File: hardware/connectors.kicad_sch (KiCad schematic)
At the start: 0 parts

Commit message: connectors - added, buses - todo
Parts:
- added J3: PWM1, symbol Connector_Generic:Conn_01x03
- added J5: PWM2, symbol Connector_Generic:Conn_01x03
- added J6: POWER & CAN & SPI2, symbol Connector_Generic:Conn_02x10_Top_Bottom
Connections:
- new net +5V: J3.3 (Pin_3), J5.3 (Pin_3)
- new net +6V6S1: J6.6 (Pin_6)
- new net +6V6S2: J6.7 (Pin_7)
- new net CAN_H: J6.14 (Pin_14)
- new net CAN_L: J6.4 (Pin_4)
- new net GND: J3.1 (Pin_1), J5.1 (Pin_1), J6.10 (Pin_10), J6.18 (Pin_18), J6.19 (Pin_19), J6.20 (Pin_20)
- new net PWM1: J3.2 (Pin_2)
- new net SPI2_MISO: J6.9 (Pin_9)
- new net SPI2_MOSI: J6.8 (Pin_8)
- new net SPI2_SCK: J6.16 (Pin_16)
- new net VCC: J6.1 (Pin_1), J6.11 (Pin_11), J6.12 (Pin_12), J6.13 (Pin_13), J6.2 (Pin_2), J6.3 (Pin_3)
- no-connect marks 0 -> 3
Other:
- note added: "POWER & CAN & SPI2"
- note added: "PWM"

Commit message: Poprawione busy, brak errorow
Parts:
- removed J6: POWER & CAN & SPI2, symbol Connector_Generic:Conn_02x10_Top_Bottom
- added C18: 10n, Capacitor_SMD:C_0603_1608Metric_Pad1.08x0.95mm_HandSolder, symbol Device:C_Small
- added J1: USB_C_Receptacle_USB2.0_14P, symbol Connector:USB_C_Receptacle_USB2.0_14P
- added J2: FTSH-107-01-L-DV-K-A, FTSH-107-XX-YYY-DV-K-A, symbol FTSH-107-01-L-DV-K-A:FTSH-107-01-L-DV-K-A
- added J7: POWER & CAN & SPI2, symbol Connector_Generic:Conn_02x06_Odd_Even
- added R2, R3: 5k1, symbol Device:R_Small
- added TP9: TP_VBUS, symbol Connector:TestPoint_Small
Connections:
- net +6V6S1: now also J3.3 (Pin_3), J7.3 (Pin_3)
- net +6V6S2: now also J5.3 (Pin_3), J7.5 (Pin_5)
- net CAN_H: now also J7.6 (Pin_6)
- net CAN_L: now also J7.4 (Pin_4)
- net GND: now also C18.2, J1.A1 (GND), J1.A12 (GND), J1.B1 (GND), J1.B12 (GND), J2.11, J2.5, J2.7, J7.11 (Pin_11), J7.12 (Pin_12), R2.2, R3.1
- net VCC: now also J7.1 (Pin_1), J7.2 (Pin_2)
- net 2: now reaches J5.2 (Pin_2)
- removed net +5V: J3.3 (Pin_3), J5.3 (Pin_3)
- net PWM1 renamed 1
- new net: C18.1, J1.S1 (SHIELD)
- new net +3V3: J2.3
- new net CLK: J2.6
- new net D+: J1.A6 (D+), J1.B6 (D+)
- new net D-: J1.A7 (D-), J1.B7 (D-)
- new net DIO: J2.4
- new net MISO: J7.7 (Pin_7)
- new net MOSI: J7.9 (Pin_9)
- new net RST: J2.12
- new net RX: J2.13
- new net SCK: J7.10 (Pin_10)
- new net TX: J2.14
- new net USB_CC1: J1.A5 (CC1), R2.1
- new net USB_CC2: J1.B5 (CC2), R3.2
- new net VBUS: J1.A4 (VBUS), J1.A9 (VBUS), J1.B4 (VBUS), J1.B9 (VBUS), TP9.1
- no-connect marks 3 -> 6
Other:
- note added: "PROGRAMATOR"
- note added: "USB"
- moved on the sheet: J3, J5

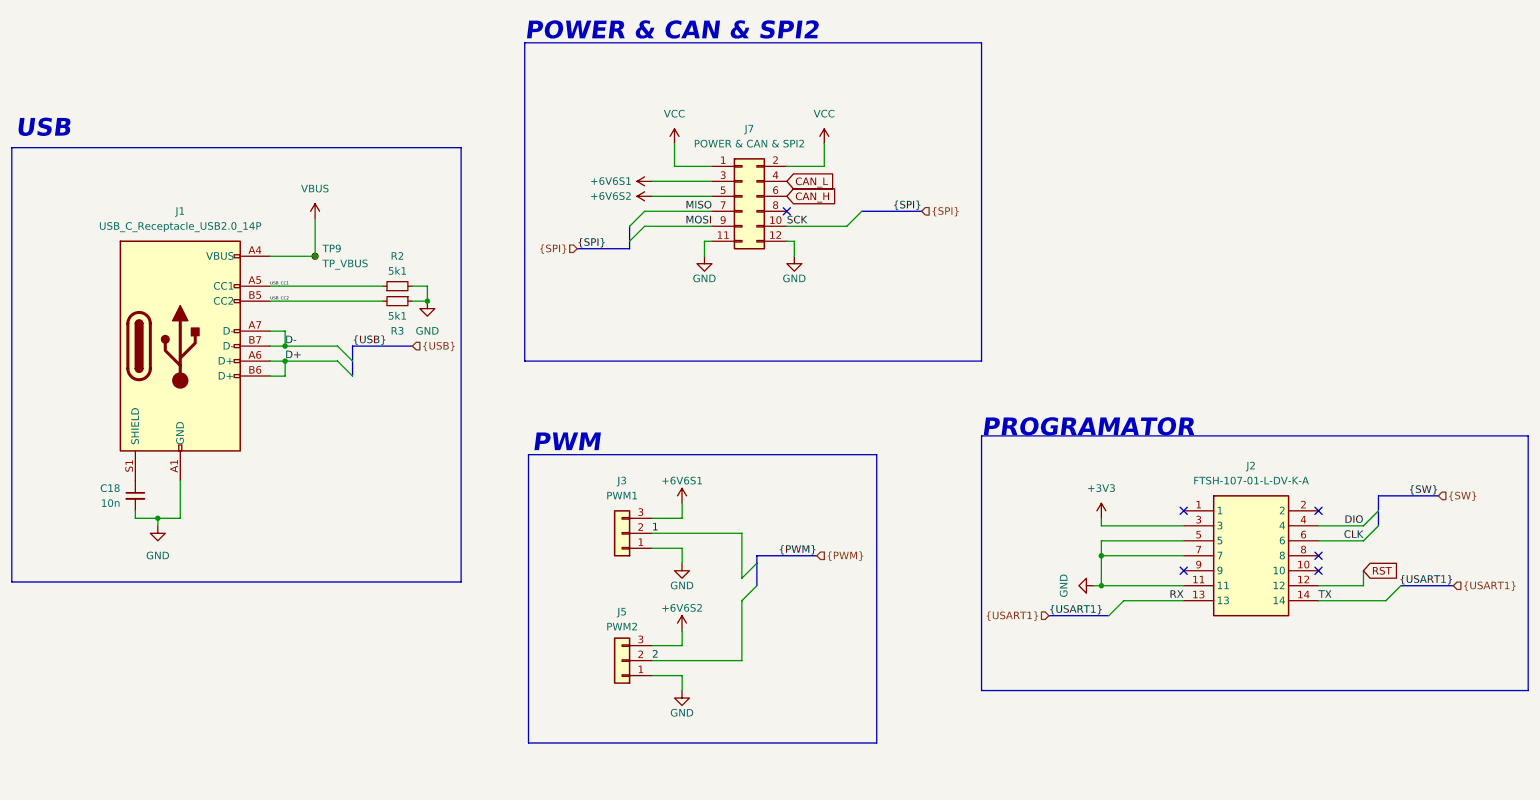
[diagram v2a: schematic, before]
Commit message: Footprints addes beside PWM connectors
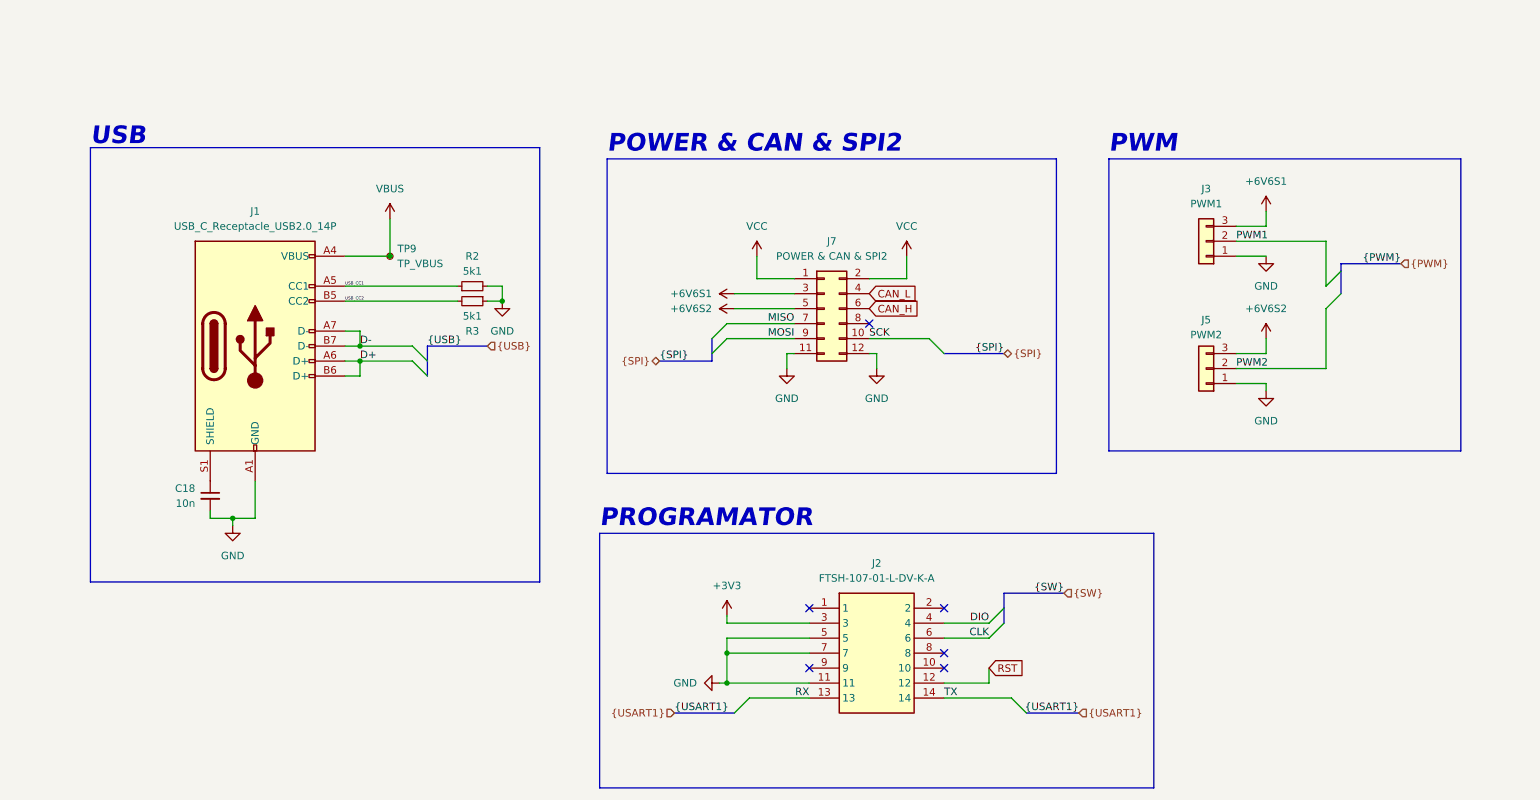
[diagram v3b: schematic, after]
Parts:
- J1: footprint (none) -> Connector_USB:USB_C_Receptacle_JAE_DX07S024WJ3R400
- J2: footprint FTSH-107-XX-YYY-DV-K-A -> SamacSys_Parts:FTSH-107-XX-YYY-DV-K-A
- J7: footprint (none) -> Connector_IDC:IDC-Header_2x06_P2.54mm_Vertical_SMD
- R2, R3: footprint (none) -> Resistor_SMD:R_0603_1608Metric_Pad0.98x0.95mm_HandSolder
- TP9: footprint (none) -> TestPoint:TestPoint_Pad_1.0x1.0mm
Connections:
- net 1 renamed PWM1
- net 2 renamed PWM2
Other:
- moved on the sheet: C18, J1, J2, J3, J5, J7, R2, R3, TP9

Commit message: PWM conns added
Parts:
- J3, J5: footprint (none) -> Connector_PinHeader_2.54mm:PinHeader_1x03_P2.54mm_Horizontal
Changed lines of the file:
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@@
 			)
 		)
-		(property "Footprint" ""
+		(property "Footprint" "Connector_PinHeader_2.54mm:PinHeader_1x03_P2.54mm_Horizontal"
 			(at 223.52 80.01 0)
 			(effects
@@
 			)
 		)
-		(property "Footprint" ""
+		(property "Footprint" "Connector_PinHeader_2.54mm:PinHeader_1x03_P2.54mm_Horizontal"
 			(at 223.52 58.42 0)
 			(effects

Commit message: Table updated- fuses and conns still not added
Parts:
- C18: Mouser Price/Stock (none) -> https://www.mouser.pl/ProductDetail/KEMET/C0603X103J4HACAUT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
- J1: footprint Connector_USB:USB_C_Receptacle_JAE_DX07S024WJ3R400 -> SamacSys_Parts:DX07S024WJ3R400; Mouser Price/Stock (none) -> https://www.mouser.pl/ProductDetail/JAE-Electronics/DX07S02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
- R2, R3: Mouser Price/Stock (none) -> https://www.mouser.pl/ProductDetail/Vishay-Dale/CRCW06035K1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
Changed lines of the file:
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@@
 			)
 		)
-		(property "Datasheet" "~"
+		(property "Datasheet" "https://www.vishay.com/docs/20035/dcrcwe3.pdf"
 			(at 99.06 66.04 0)
 			(effects
@@
 		)
 		(property "Description" "Resistor, small symbol"
+			(at 99.06 66.04 0)
+			(effects
+				(font
+					(size 1.27 1.27)
+				)
+				(hide yes)
+			)
+		)
+		(property "Mouser Price/Stock" "https://www.mouser.pl/ProductDetail/Vishay-Dale/CRCW06035K10FKEC?qs=sGAEpiMZZMtlubZbdhIBIKbhzOdzan%2FGt7ImYW9MzNM%3D"
 			(at 99.06 66.04 0)
 			(effects
@@
 			)
 		)
-		(property "Datasheet" "~"
+		(property "Datasheet" "https://www.mouser.pl/datasheet/2/447/KEM_C1063_X8R_FT_CAP_SMD-3316286.pdf"
 			(at 54.61 101.6 0)
 			(effects
@@
 		)
 		(property "Description" "Unpolarized capacitor, small symbol"
+			(at 54.61 101.6 0)
+			(effects
+				(font
+					(size 1.27 1.27)
+				)
+				(hide yes)
+			)
+		)
+		(property "Mouser Price/Stock" "https://www.mouser.pl/ProductDetail/KEMET/C0603X103J4HACAUTO?qs=rrS6PyfT74eN%2FOGgR5%2FPZQ%3D%3D"
 			(at 54.61 101.6 0)
 			(effects
@@
 			)
 		)
-		(property "Datasheet" "~"
+		(property "Datasheet" "https://www.vishay.com/docs/20035/dcrcwe3.pdf"
 			(at 99.06 68.58 0)
 			(effects
@@
 		)
 		(property "Description" "Resistor, small symbol"
+			(at 99.06 68.58 0)
+			(effects
+				(font
+					(size 1.27 1.27)
+				)
+				(hide yes)
+			)
+		)
+		(property "Mouser Price/Stock" "https://www.mouser.pl/ProductDetail/Vishay-Dale/CRCW06035K10FKEC?qs=sGAEpiMZZMtlubZbdhIBIKbhzOdzan%2FGt7ImYW9MzNM%3D"
 			(at 99.06 68.58 0)
 			(effects
@@
 			)
 		)
-		(property "Footprint" "Connector_USB:USB_C_Receptacle_JAE_DX07S024WJ3R400"
+		(property "Footprint" "SamacSys_Parts:DX07S024WJ3R400"
 			(at 66.04 76.2 0)
 			(effects
@@
 			)
 		)
-		(property "Datasheet" "https://www.usb.org/sites/default/files/documents/usb_type-c.zip"
+		(property "Datasheet" "https://www.mouser.pl/datasheet/2/206/JAEI_S_A0002811482_1-2550784.pdf"
 			(at 66.04 76.2 0)
 			(effects
@@
 			(at 62.23 76.2 0)
 			(effects
+				(font
+					(size 1.27 1.27)
+				)
+				(hide yes)
+			)
+		)
+		(property "Mouser Price/Stock" "https://www.mouser.pl/ProductDetail/JAE-Electronics/DX07S024WJ3R400?qs=Ps1sUSMe7kmTGGC30IqfqQ%3D%3D"
+			(at 62.23 76.2 0)
+			(effects

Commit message: All footprints added
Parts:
- J3, J5: footprint Connector_PinHeader_2.54mm:PinHeader_1x03_P2.54mm_Horizontal -> SamacSys_Parts:HDRV3W64P0X254_1X3_762X254X864P; Mouser Price/Stock (none) -> https://www.tme.eu/pl/details/m20-9990346/zlacza-sygnalowe-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
- J7: footprint Connector_IDC:IDC-Header_2x06_P2.54mm_Vertical_SMD -> SamacSys_Parts:SHDR12W64P254X254_2X6_2286X895X915P; Mouser Price/Stock (none) -> https://www.tme.eu/pl/details/t821-1-12-s1/zlacza-idc/amphe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
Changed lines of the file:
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@@
 			)
 		)
-		(property "Footprint" "Connector_PinHeader_2.54mm:PinHeader_1x03_P2.54mm_Horizontal"
+		(property "Footprint" "SamacSys_Parts:HDRV3W64P0X254_1X3_762X254X864P"
 			(at 223.52 80.01 0)
 			(effects
@@
 			)
 		)
-		(property "Datasheet" "~"
+		(property "Datasheet" "https://www.tme.eu/Document/52c5536d604d4472a828deca8b13b729/M20-9990346.pdf"
 			(at 223.52 80.01 0)
 			(effects
@@
 		)
 		(property "Description" "Generic connector, single row, 01x03, script generated (kicad-library-utils/schlib/autogen/connector/)"
+			(at 223.52 80.01 0)
+			(effects
+				(font
+					(size 1.27 1.27)
+				)
+				(hide yes)
+			)
+		)
+		(property "Mouser Price/Stock" "https://www.tme.eu/pl/details/m20-9990346/zlacza-sygnalowe-raster-2-54mm/harwin/"
 			(at 223.52 80.01 0)
 			(effects
@@
 			)
 		)
-		(property "Footprint" "Connector_PinHeader_2.54mm:PinHeader_1x03_P2.54mm_Horizontal"
+		(property "Footprint" "SamacSys_Parts:HDRV3W64P0X254_1X3_762X254X864P"
 			(at 223.52 58.42 0)
 			(effects
@@
 			)
 		)
-		(property "Datasheet" "~"
+		(property "Datasheet" "https://www.tme.eu/Document/52c5536d604d4472a828deca8b13b729/M20-9990346.pdf"
 			(at 223.52 58.42 0)
 			(effects
@@
 		)
 		(property "Description" "Generic connector, single row, 01x03, script generated (kicad-library-utils/schlib/autogen/connector/)"
+			(at 223.52 58.42 0)
+			(effects
+				(font
+					(size 1.27 1.27)
+				)
+				(hide yes)
+			)
+		)
+		(property "Mouser Price/Stock" "https://www.tme.eu/pl/details/m20-9990346/zlacza-sygnalowe-raster-2-54mm/harwin/"
 			(at 223.52 58.42 0)
 			(effects
@@
 			)
 		)
-		(property "Footprint" "Connector_IDC:IDC-Header_2x06_P2.54mm_Vertical_SMD"
+		(property "Footprint" "SamacSys_Parts:SHDR12W64P254X254_2X6_2286X895X915P"
 			(at 158.75 69.85 0)
 			(effects
@@
 			)
 		)
-		(property "Datasheet" "~"
+		(property "Datasheet" "https://www.tme.eu/Document/7d9961e5e60ab95d248a27b27276cc23/t821.pdf"
 			(at 158.75 69.85 0)
 			(effects
@@
 			(at 158.75 69.85 0)
 			(effects
+				(font
+					(size 1.27 1.27)
+				)
+				(hide yes)
+			)
+		)
+		(property "Mouser Price/Stock" "https://www.tme.eu/pl/details/t821-1-12-s1/zlacza-idc/amphenol-communications-solutions/t821112a1s100ceu/"
+			(at 158.75 69.85 0)
+			(effects

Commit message: pcb scheme update - general/basic aligment
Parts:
- removed J1: USB_C_Receptacle_USB2.0_14P, SamacSys_Parts:DX07S024WJ3R400, symbol Connector:USB_C_Receptacle_USB2.0_14P
- removed J2: FTSH-107-01-L-DV-K-A, SamacSys_Parts:FTSH-107-XX-YYY-DV-K-A, symbol FTSH-107-01-L-DV-K-A:FTSH-107-01-L-DV-K-A
- added J1: USB_C_Receptacle_USB2.0_16P, SamacSys_Parts:USB4145030230C, symbol Connector:USB_C_Receptacle_USB2.0_16P
- added J2: FTSH-107-01-L-D-K, SamacSys_Parts:FTSH-107-XX-YYY-D-K, symbol SamacSys_Parts:FTSH-107-01-L-D-K
- renumbered C18 to C31, J7 to J3, J3 to J4, R2 to R12, R3 to R13, TP9 to TP13
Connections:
- net +3V3: now also J2.3
- net CLK: now also J2.6
- net D+: now also J1.A6 (D+), J1.B6 (D+)
- net D-: now also J1.A7 (D-), J1.B7 (D-)
- net DIO: now also J2.4
- net GND: now also J1.A1 (GND), J1.A12 (GND), J1.B1 (GND), J1.B12 (GND), J2.11, J2.5, J2.7
- net RST: now also J2.12
- net RX: now also J2.13
- net TX: now also J2.14
- net USB_CC1: now also J1.A5 (CC1)
- net USB_CC2: now also J1.B5 (CC2)
- net VBUS: now also J1.A4 (VBUS), J1.A9 (VBUS), J1.B4 (VBUS), J1.B9 (VBUS)
- net at C31.1: now also J1.S1 (SHIELD)
- no-connect marks 6 -> 8

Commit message: Items assebled
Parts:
- removed C31: 10n, Capacitor_SMD:C_0603_1608Metric_Pad1.08x0.95mm_HandSolder, symbol Device:C_Small
- removed J1: USB_C_Receptacle_USB2.0_16P, SamacSys_Parts:USB4145030230C, symbol Connector:USB_C_Receptacle_USB2.0_16P
- added J1: USB-C_GCT_USB4145-03-0070-C, SamacSys_Parts:USB4145030230C, symbol USB-C_GCT_USB4145-03-0070-C:USB-C_GCT_USB4145-03-0070-C
- renumbered TP13 to T13
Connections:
- net CLK: now also J2.4; no longer J2.6
- net D+: now also J1.B6 (D_{B}+), J1.B7 (D_{B}-)
- net D-: now also J1.A6 (D_{A}+), J1.A7 (D_{A}-)
- net DIO: now also J2.6; no longer J2.4
- net GND: now also J1.A1 (GND), J1.A12 (GND), J1.B1 (GND), J1.B12 (GND), J1.SH
- net USB_CC1: now also J1.A5 (CC_{1})
- net USB_CC2: now also J1.B5 (CC_{2})
- net VBUS: now also J1.A4 (VBUS), J1.A9 (VBUS), J1.B4 (VBUS), J1.B9 (VBUS)
- net CAN_H: no longer names the net of J3.6 (Pin_6)
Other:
- moved on the sheet: R12, R13, T13
